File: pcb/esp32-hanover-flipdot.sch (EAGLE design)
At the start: 28 parts, among them J1 DC-005, J2 HANOVER, J3 FTDI, Q1 NCE3407A, Q2 S9013, U1 ESP32-PICO-D4, U2 CJA1117B-3.3-SOT89, U3 LM2576SX-5.0/NOPB

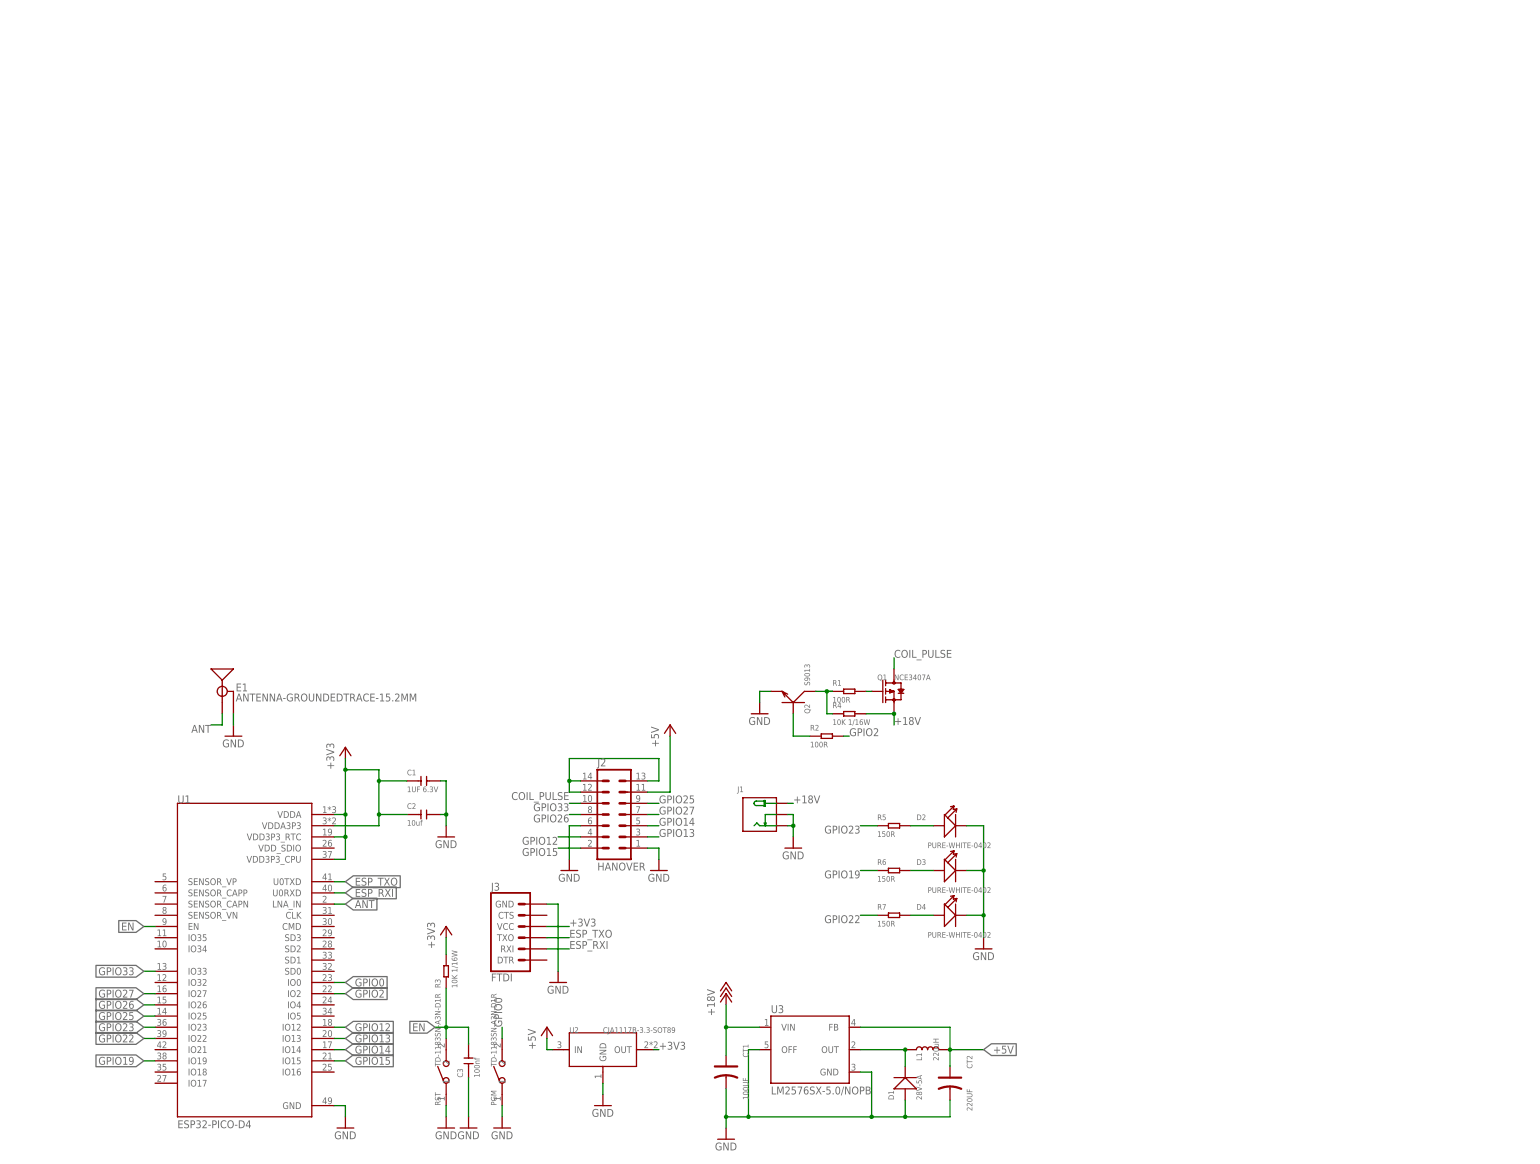
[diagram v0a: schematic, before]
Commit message: pcb: Add Ethernet and PoE
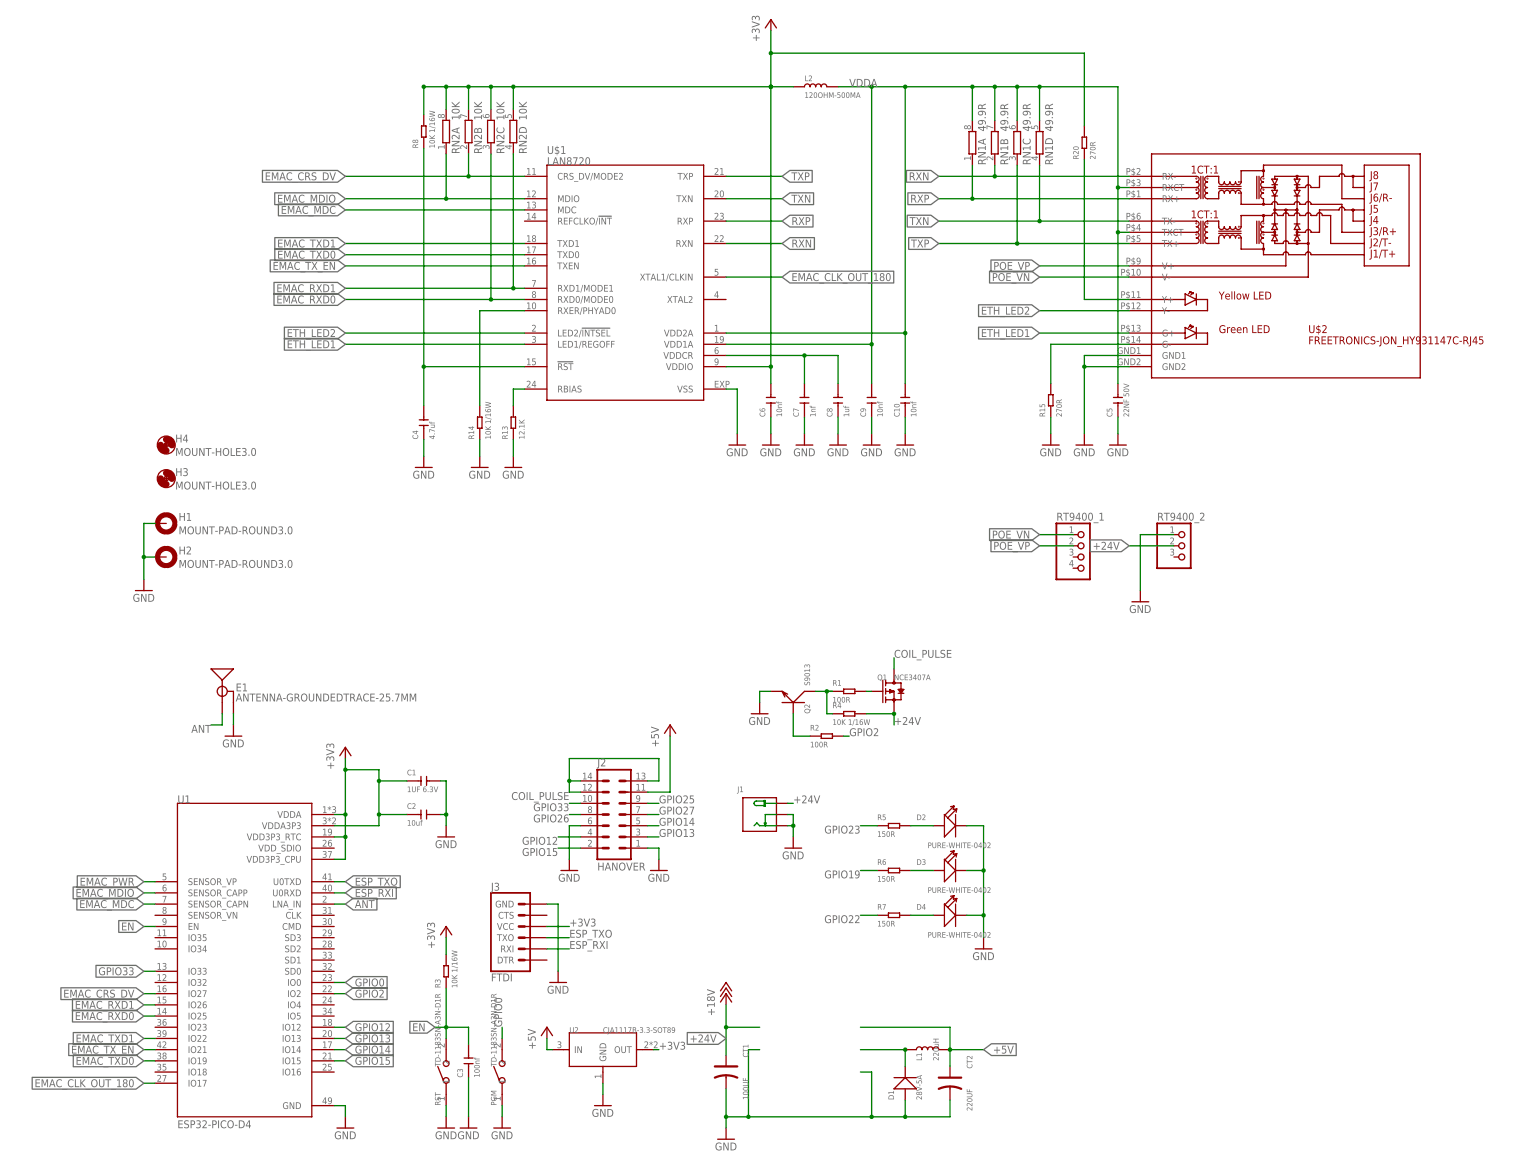
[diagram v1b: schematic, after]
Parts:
- removed U3: LM2576SX-5.0/NOPB, LM2576 (1):LM2576S
- added C10, C6, C9: 10nf, OPL_Capacitor:CERAMIC-10NF-50V-10%-X7R(0402)
- added C4: 4.7uf, OPL_Capacitor:CERAMIC-4.7UF-6.3V-20%-X5R(0402)
- added C5: 22NF 50V, OPL_Capacitor:CERAMIC-22NF-50V-10%-X7R(0402)
- added C7: 1nf, OPL_Capacitor:CERAMIC-1NF-50V-10%-X7R(0402)
- added C8: 1uf, OPL_Capacitor:CERAMIC-1UF-10V-10%-X5R(0402)
- added H1, H2: MOUNT-PAD-ROUND3.0, holes:MOUNT-PAD-ROUND3.0
- added H3, H4: MOUNT-HOLE3.0, holes:MOUNT-HOLE3.0
- added L2: 120OHM-500MA, OPL_Ferrite_and_Magnetic_Bead:SMD-FERRITE-CHIP-120-OHM-500MA(0603)
- added R13: 12.1K, OPL_Resistor:SMD-RES-12K-1%-1/16W(0402)
- added R14, R8: 10K 1/16W, OPL_Resistor:SMD-RES-10K-1%-1/16W(0402)
- added R15: 270R, OPL_Resistor:SMD-RES-270R-1%-1/16W(0402)
- added R20: 270R, OPL_Resistor:SMD-RES-180R-1%-1/16W(0402)
- added RN1: 49.9R, resistor-dil:4R-NYC124
- added RN2: 10K, resistor-dil:4R-NYC124
- added RT9400_1: (no value), pinhead:PINHD-1X4
- added RT9400_2: (no value), pinhead:PINHD-1X3
- added U$1: LAN8720, microchip-smsc-lan8720:LAN8720
- added U$2: FREETRONICS-JON_HY931147C-RJ45, parts:FREETRONICS-JON_HY931147C-RJ45
- E1: value ANTENNA-GROUNDEDTRACE-15.2MM -> ANTENNA-GROUNDEDTRACE-25.7MM; device SparkFun-RF:ANTENNA-GROUNDEDTRACE-15.2MM -> SparkFun-RF:ANTENNA-GROUNDEDTRACE-25.7MM
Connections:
- removed net +18V: CT1.+, J1.+, Q1.S, R4.2, U3.VIN
- new net +24V: CT1.+, J1.+, Q1.S, R4.2, RT9400_2.2
- new net EMAC_CLK_OUT_180: U$1.XTAL1/CLKIN, U1.IO17
- new net EMAC_CRS_DV: RN2B.1, U$1.CRS_DV/MODE2, U1.IO27
- new net EMAC_MDC: U$1.MDC, U1.SENSOR_CAPN
- new net EMAC_MDIO: RN2A.1, U$1.MDIO, U1.SENSOR_CAPP
- new net EMAC_PWR: U1.SENSOR_VP
- new net EMAC_RXD0: RN2C.1, U$1.RXD0/MODE0, U1.IO25
- new net EMAC_RXD1: RN2D.1, U$1.RXD1/MODE1, U1.IO26
- new net EMAC_TXD0: U$1.TXD0, U1.IO19
- new net EMAC_TXD1: U$1.TXD1, U1.IO22
- new net EMAC_TX_EN: U$1.TXEN, U1.IO21
- new net ETH_LED1: U$1.LED1/REGOFF, U$2.G+
- new net ETH_LED2: U$1.LED2/!INTSEL, U$2.Y-
- new net N$10: R15.2, U$2.G-
- new net N$13: C7.2, C8.2, U$1.VDDCR
- new net N$14: R20.1, U$2.Y+
- new net N$16: C4.2, R8.1, U$1.!RST
- new net N$8: R14.2, U$1.RXER/PHYAD0
- new net N$9: R13.2, U$1.RBIAS
- new net POE_VN: RT9400_1.1, U$2.V-
- new net POE_VP: RT9400_1.2, U$2.V+
- new net RXN: RN1B.1, U$1.RXN, U$2.RX-
- new net RXP: RN1A.1, U$1.RXP, U$2.RX+
- new net TXN: RN1D.1, U$1.TXN, U$2.TX-
- new net TXP: RN1C.1, U$1.TXP, U$2.TX+
- new net VDDA: C10.2, C5.2, C9.2, L2.2, RN1A.2, RN1B.2, RN1C.2, RN1D.2, U$1.VDD1A, U$1.VDD2A, U$2.RXCT, U$2.TXCT
- net +3V3: now also C6.2, L2.1, R20.2, R8.2, RN2A.2, RN2B.2, RN2C.2, RN2D.2, U$1.VDDIO
- net +5V: no longer U3.FB
- net GND: now also C10.1, C4.1, C5.1, C6.1, C7.1, C8.1, C9.1, H1.MOUNT, H2.MOUNT, R13.1, R14.1, R15.1, RT9400_2.1, U$1.VSS, U$2.GND1, U$2.GND2; no longer U3.GND, U3.OFF
- net GPIO19: no longer U1.IO19
- net GPIO22: no longer U1.IO22
- net GPIO23: no longer U1.IO23
- net GPIO25: no longer U1.IO25
- net GPIO26: no longer U1.IO26
- net GPIO27: no longer U1.IO27
- net N$4: no longer U3.OUT
